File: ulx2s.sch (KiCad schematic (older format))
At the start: 0 parts

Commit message: flash chip
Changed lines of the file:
@@
 $Descr A4 11693 8268
 encoding utf-8
-Sheet 1 5
+Sheet 1 6
 Title ""
 Date ""
@@
 F1 "blinkey.sch" 60
 $EndSheet
+$Sheet
+S 8650 5400 600  400
+U 5A12F4E1
+F0 "flash" 60
+F1 "flash.sch" 60
+$EndSheet
 $EndSCHEMATC

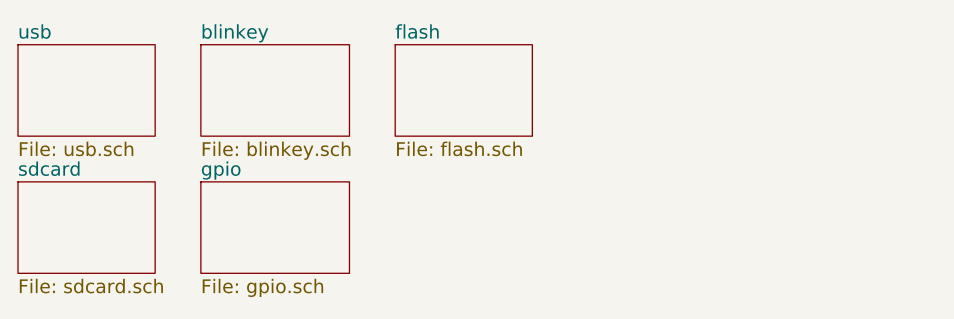
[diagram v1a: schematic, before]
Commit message: fpga chip placed in the schematic "fpga" sheet and on the PCB.
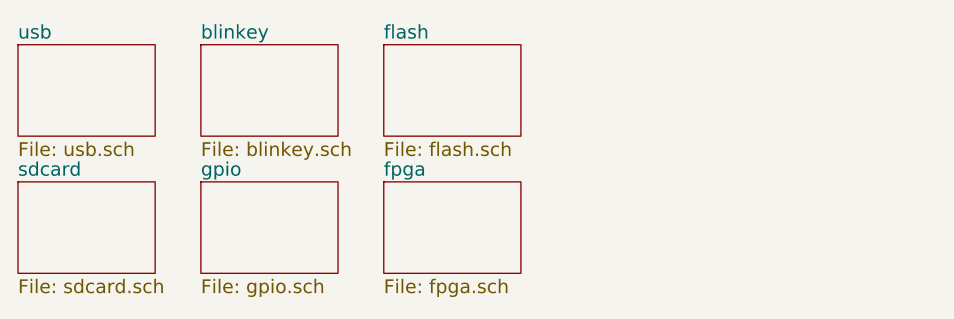
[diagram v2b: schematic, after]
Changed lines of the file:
@@
 LIBS:contrib
 LIBS:valves
+LIBS:lfxp2-xe-xtn144x
 LIBS:ulx2s-cache
 EELAYER 25 0
@@
 $Descr A4 11693 8268
 encoding utf-8
-Sheet 1 6
+Sheet 1 7
 Title ""
 Date ""
@@
 $EndSheet
 $Sheet
-S 7800 6000 650  400
+S 7800 6000 600  400
 U 5A12C7A4
 F0 "gpio" 60
@@
 $EndSheet
 $Sheet
-S 7800 5400 650  400
+S 7800 5400 600  400
 U 5A12D02C
 F0 "blinkey" 60
@@
 $EndSheet
 $Sheet
-S 8650 5400 600  400
+S 8600 5400 600  400
 U 5A12F4E1
 F0 "flash" 60
 F1 "flash.sch" 60
 $EndSheet
+$Sheet
+S 8600 6000 600  400
+U 5A13EEF2
+F0 "fpga" 60
+F1 "fpga.sch" 60
+$EndSheet
 $EndSCHEMATC

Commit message: SRAM chip (not the correct one AS6C8016 but similar AS6C1616 which was readily available in kicad library)
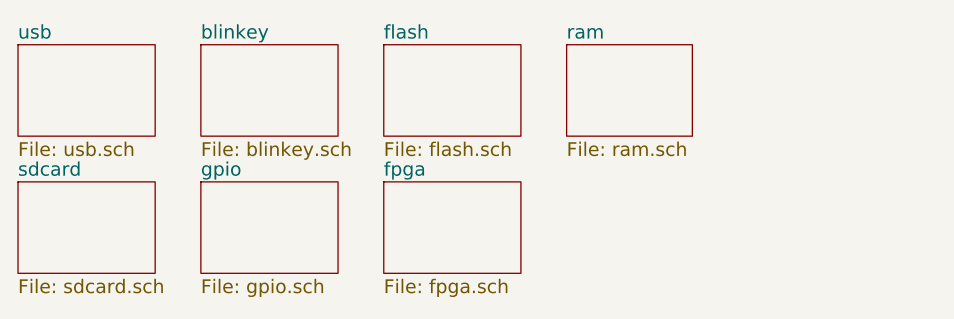
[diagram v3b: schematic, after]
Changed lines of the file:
@@
 $Descr A4 11693 8268
 encoding utf-8
-Sheet 1 7
+Sheet 1 8
 Title ""
 Date ""
@@
 F1 "fpga.sch" 60
 $EndSheet
+$Sheet
+S 9400 5400 550  400
+U 5A132F2F
+F0 "ram" 60
+F1 "ram.sch" 60
+$EndSheet
 $EndSCHEMATC

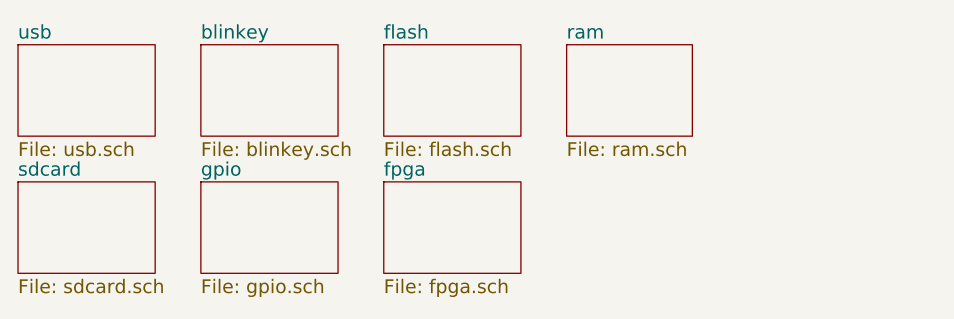
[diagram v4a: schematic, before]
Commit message: voltage regulators
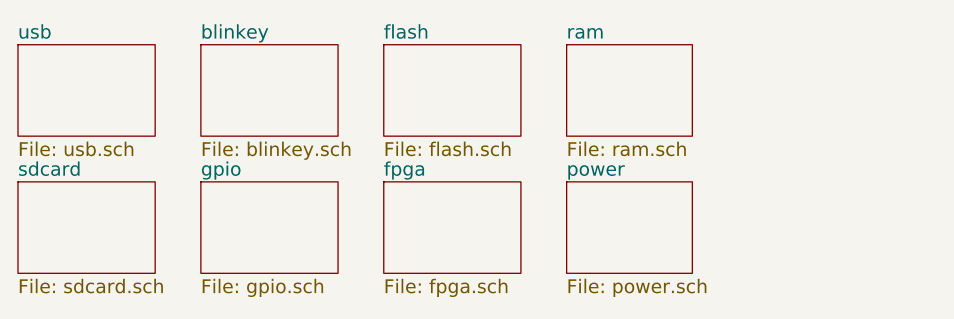
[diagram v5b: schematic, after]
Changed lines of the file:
@@
 $Descr A4 11693 8268
 encoding utf-8
-Sheet 1 8
+Sheet 1 9
 Title ""
 Date ""
@@
 F1 "ram.sch" 60
 $EndSheet
+$Sheet
+S 9400 6000 550  400
+U 5A1338E7
+F0 "power" 60
+F1 "power.sch" 60
+$EndSheet
 $EndSCHEMATC

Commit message: audio jack placed
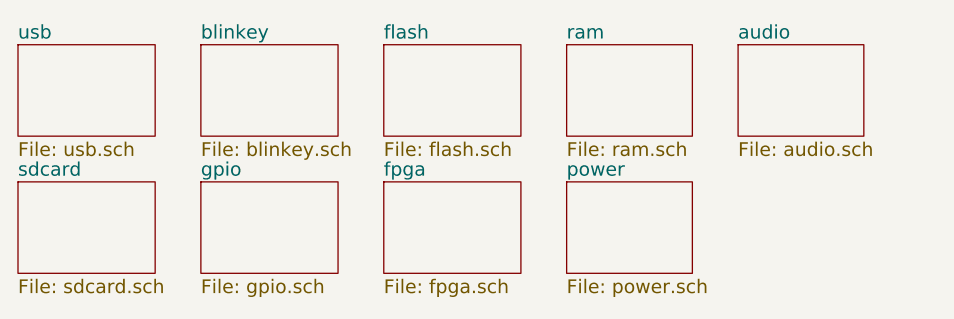
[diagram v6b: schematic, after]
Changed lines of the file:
@@
 $Descr A4 11693 8268
 encoding utf-8
-Sheet 1 9
+Sheet 1 10
 Title ""
 Date ""
@@
 F1 "power.sch" 60
 $EndSheet
+$Sheet
+S 10150 5400 550  400
+U 5A133C56
+F0 "audio" 60
+F1 "audio.sch" 60
+$EndSheet
 $EndSCHEMATC

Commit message: micro hdmi connector
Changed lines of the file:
@@
 LIBS:lfxp2-xe-xtn144x
 LIBS:ftdi
+LIBS:micro-hdmi-d
 LIBS:ulx2s-cache
 EELAYER 25 0
@@
 $Descr A4 11693 8268
 encoding utf-8
-Sheet 1 10
+Sheet 1 11
 Title ""
 Date ""
@@
 F1 "audio.sch" 60
 $EndSheet
+$Sheet
+S 10150 6000 550  400
+U 5A13439C
+F0 "gpdi" 60
+F1 "gpdi.sch" 60
+$EndSheet
 $EndSCHEMATC
